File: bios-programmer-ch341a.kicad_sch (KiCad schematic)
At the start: 50 parts, among them J1 USB_B_Micro, J2 SPI Debug, J3 I²C Debug, J4 -Banana-, J5 +Banana+, J6 ZIF16, J7 Conn_02x05_Odd_Even, J8 Conn_02x05_Odd_Even, J9 SENSE, Q1 SSM3J328R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

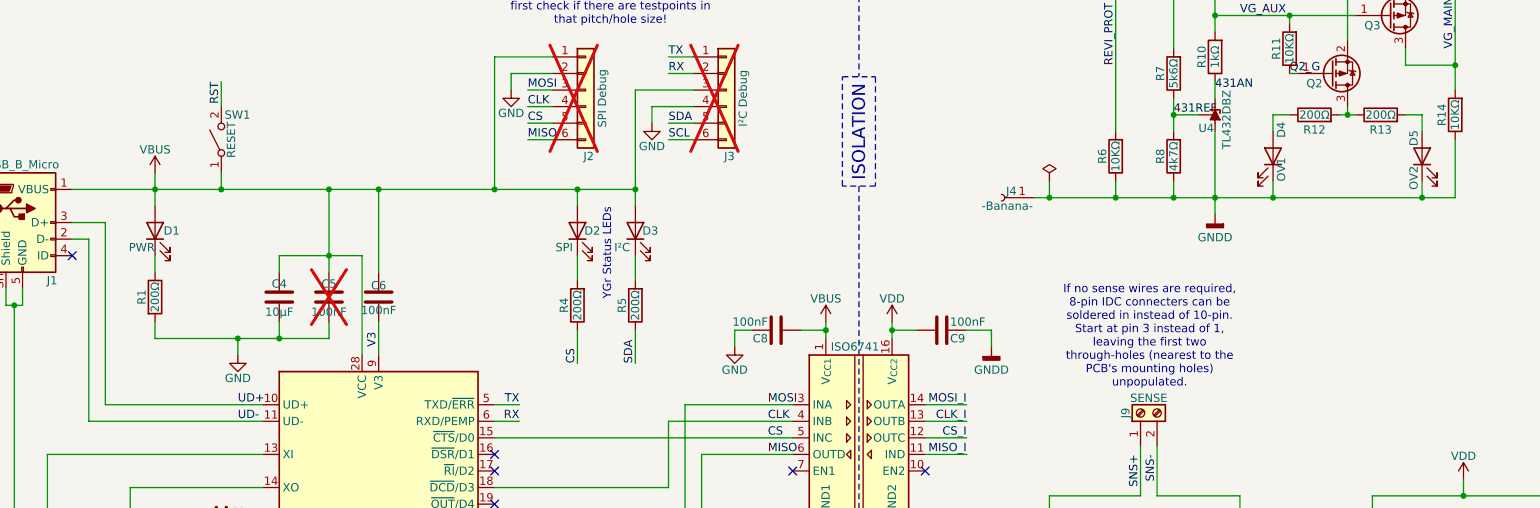
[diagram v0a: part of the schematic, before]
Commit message: PCB/SCH: separate field Label for PCB label & sort manufacturer/part #s
Using "Value" for the PCB label isn't terrible, but at the same time it's not
really "locked down" as a separate label. There's no reason Value can't be used
for something to indicate a certain message to the user in the schematics.
It's also not clear for anyone looking at the schematics that that specific
text is used on the PCB.

Splitting up removes any ambiguity.
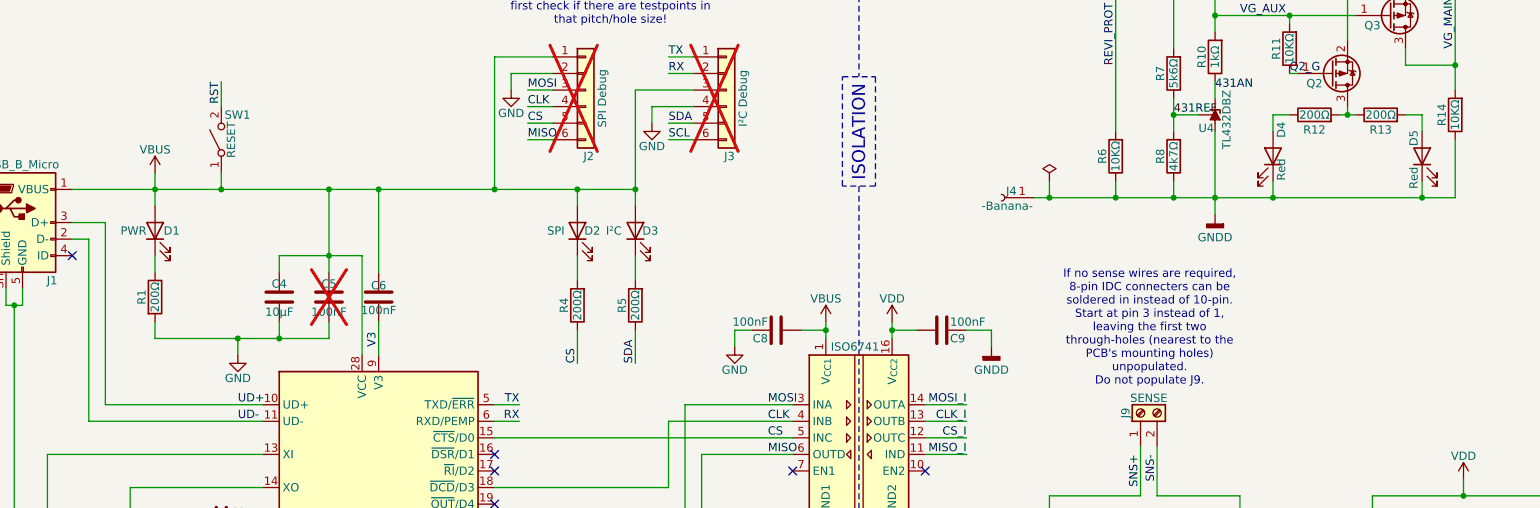
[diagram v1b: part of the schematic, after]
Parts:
- C1, C2: Manufacturer Kemet -> (none); Mfr (none) -> TODO calc; Part C0603C180F8HACAUTO -> TODO
- C3, C5, C6, C7, C8, C9: Mfr (none) -> Yageo; Part (none) -> CC0603KRX7R7BB104
- C4: Mfr (none) -> Taiyo Yuden; Part (none) -> JMK212B7106KG-T
- D1: value PWR -> TODO; Label (none) -> PWR
- D2: value SPI -> YellowGreen; Label (none) -> SPI; Mfr (none) -> Inolux; Part (none) -> HT-193UYG-5592
- D3: value I²C -> YellowGreen; Label (none) -> I²C; Mfr (none) -> Inolux; Part (none) -> HT-193UYG-5592
- D4: value OV1 -> Red
- D5: value OV2 -> Red
- J4: AltMfr1 (none) -> Schützinger; AltPart1 (none) -> 8094 TODO; Mfr (none) -> Cliff; Part (none) -> FCR7350B
- J5: AltMfr1 (none) -> Schützinger; AltPart1 (none) -> 8094 TODO; Mfr (none) -> Cliff; Part (none) -> FCR7350R
- J6: Mfr (none) -> M3
- R1, R12, R13, R4, R5: Mfr (none) -> Panasonic; Part (none) -> ERJ-3EKF2000V
- R11, R14, R6: Mfr (none) -> Yageo; Part (none) -> RC0603JR-0710KL
- SW1: value RESET -> SPST; Label (none) -> RESET
- U2: Part (none) -> ISO6741DWR
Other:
- note removed: "YGr Status LEDs"

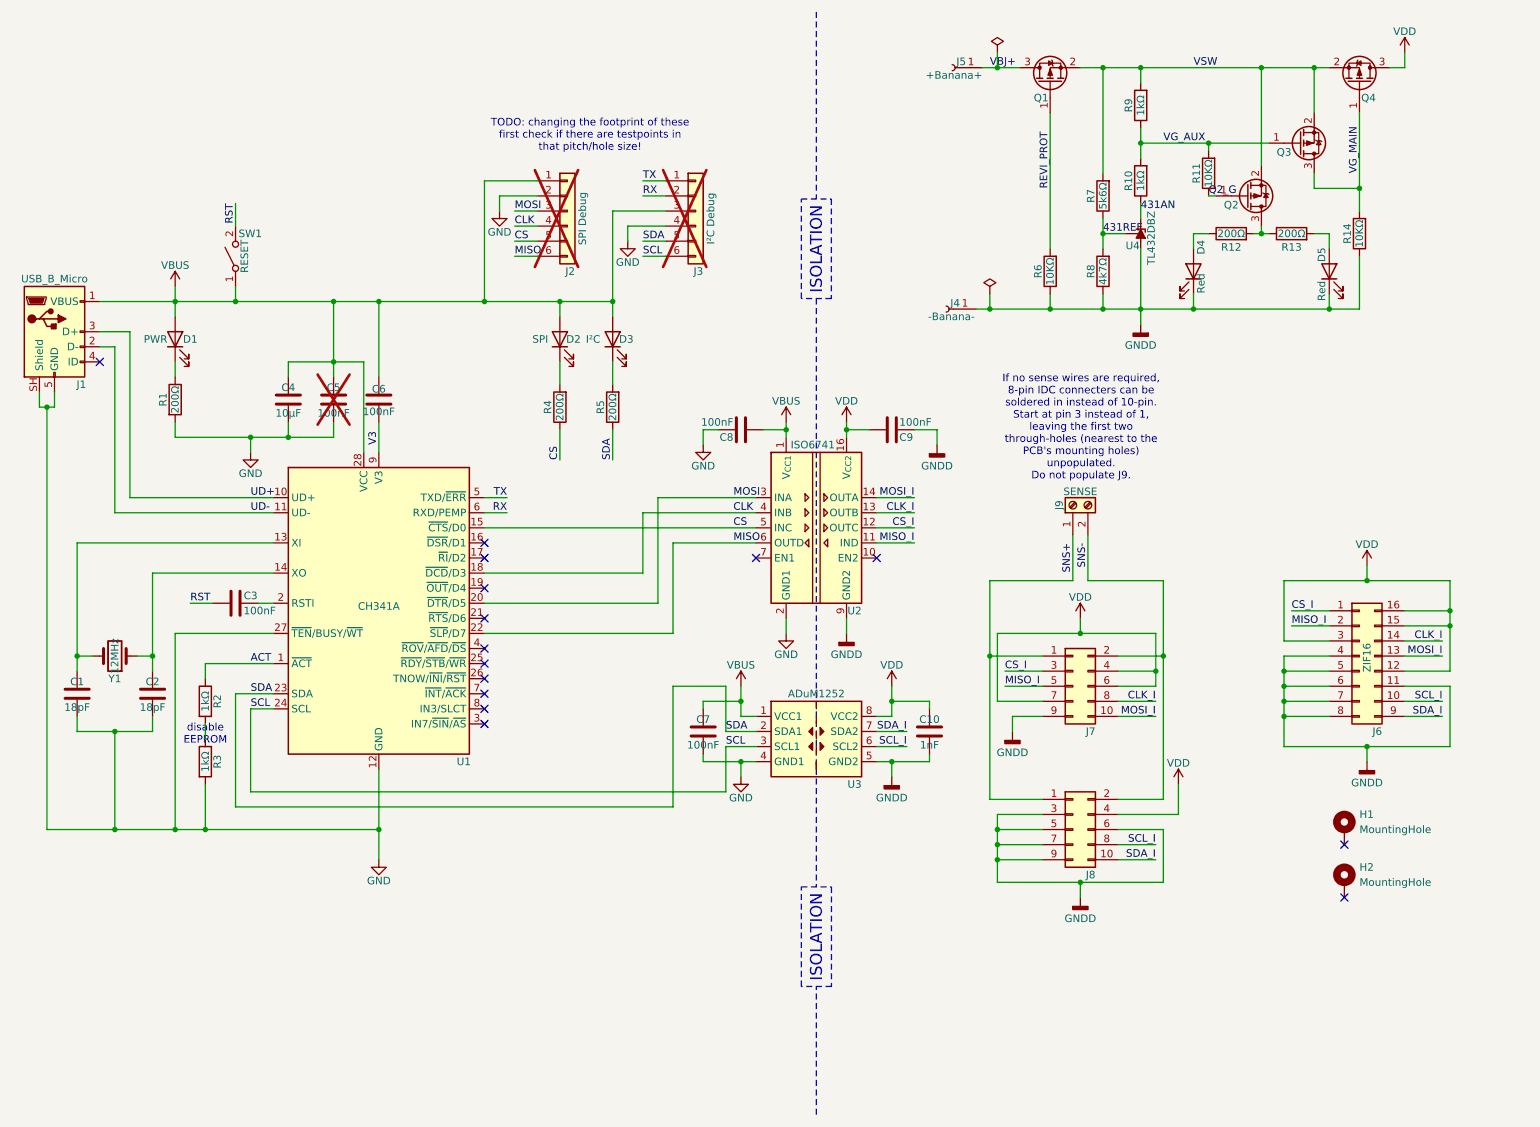
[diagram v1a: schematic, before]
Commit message: SCH: added some part numbers
Some part numbers have many possibilities, like 5% resistors. I assign these
simply based on what I have in stock, sometimes using a more expensive one that
uses up some of my (already very small) stock.
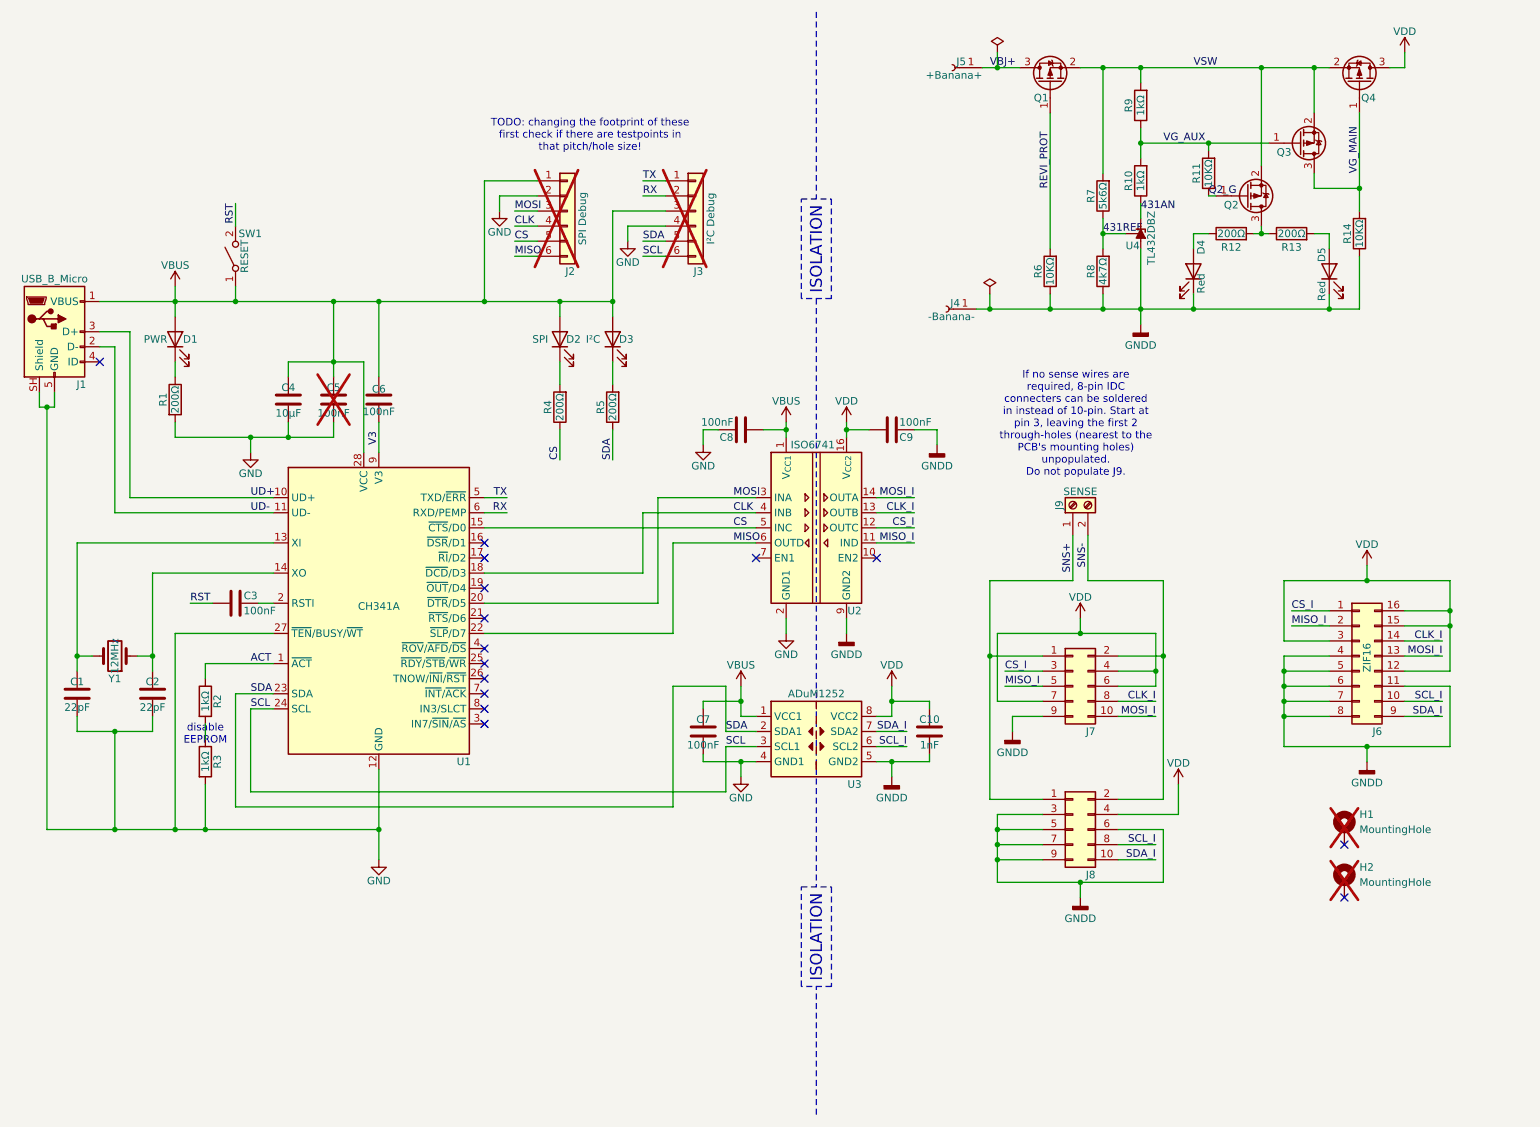
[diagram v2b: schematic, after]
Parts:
- C1, C2: value 18pF -> 22pF; AltMfr1 (none) -> Yageo; AltPart1 (none) -> CC0603GRNPO9BN220; Mfr TODO calc -> Kyocera / AVX; Part TODO -> 06035A270GAT2A
- C10: AltMfr1 (none) -> Samsung; AltPart1 (none) -> CL10B102KB8NNNC; Mfr (none) -> Murata; Part (none) -> GRM033R71H102KA12D
- D1: value TODO -> Blue; AltMfr1 (none) -> Lite-On Inc; AltPart1 (none) -> LTST-C170TBKT; Mfr (none) -> Inolux; Part (none) -> IN-S85AT5B
- D4, D5: AltMfr1 (none) -> Lite-On Inc; AltPart1 (none) -> LTST-C171KRKT; Mfr (none) -> Kingbright; Part (none) -> APT2012SURCK
- H1, H2: now not fitted
- J4: AltPart1 8094 TODO -> SWEB 8094 AU / RT
- J5: AltPart1 8094 TODO -> SWEB 8094 AU / SW
- J6: Part (none) -> 216-3340-00-0602J
- J7, J8: AltMfr1 (none) -> Wurth Elektronik; AltPart1 (none) -> 61201021721; Mfr (none) -> TE Connectivity; Part (none) -> 1761682-3
- R10, R2, R3, R9: Mfr (none) -> Royalohm; Part (none) -> CQ03WAJ0102T5E
- R7: Mfr (none) -> Susumu; Part (none) -> RG1608P-562-D-T5
- R8: Mfr (none) -> Susumu; Part (none) -> RR0816P-4641-D-65H
- SW1: Mfr (none) -> C&K; Part (none) -> PTS636SKG25SMTR LFS
- U3: Mfr (none) -> Analog Devices; Part (none) -> ADUM1252ASA+
- Y1: AltMfr1 (none) -> Abracon; AltPart1 (none) -> ABL-12.000MHZ-N2X-T; Mfr (none) -> Abracon; Part (none) -> ABL-12.000MHZ-B2

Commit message: PCB: updated sense wire connector models, added U3 (ADum) caps & more part#s
Previously I used a model which sort-of fit but already included in Kicad, now
I use an actual model of what I can expect it to look like.

The capacitors on the I2C isolator were in the datasheet, but it seems I forgot
to duplicate them. I had somehow put the 100nF & 1nF on a different side of the
isolation barrier. According to the datasheet I should have both on each side.

Also some beautification of tracks.
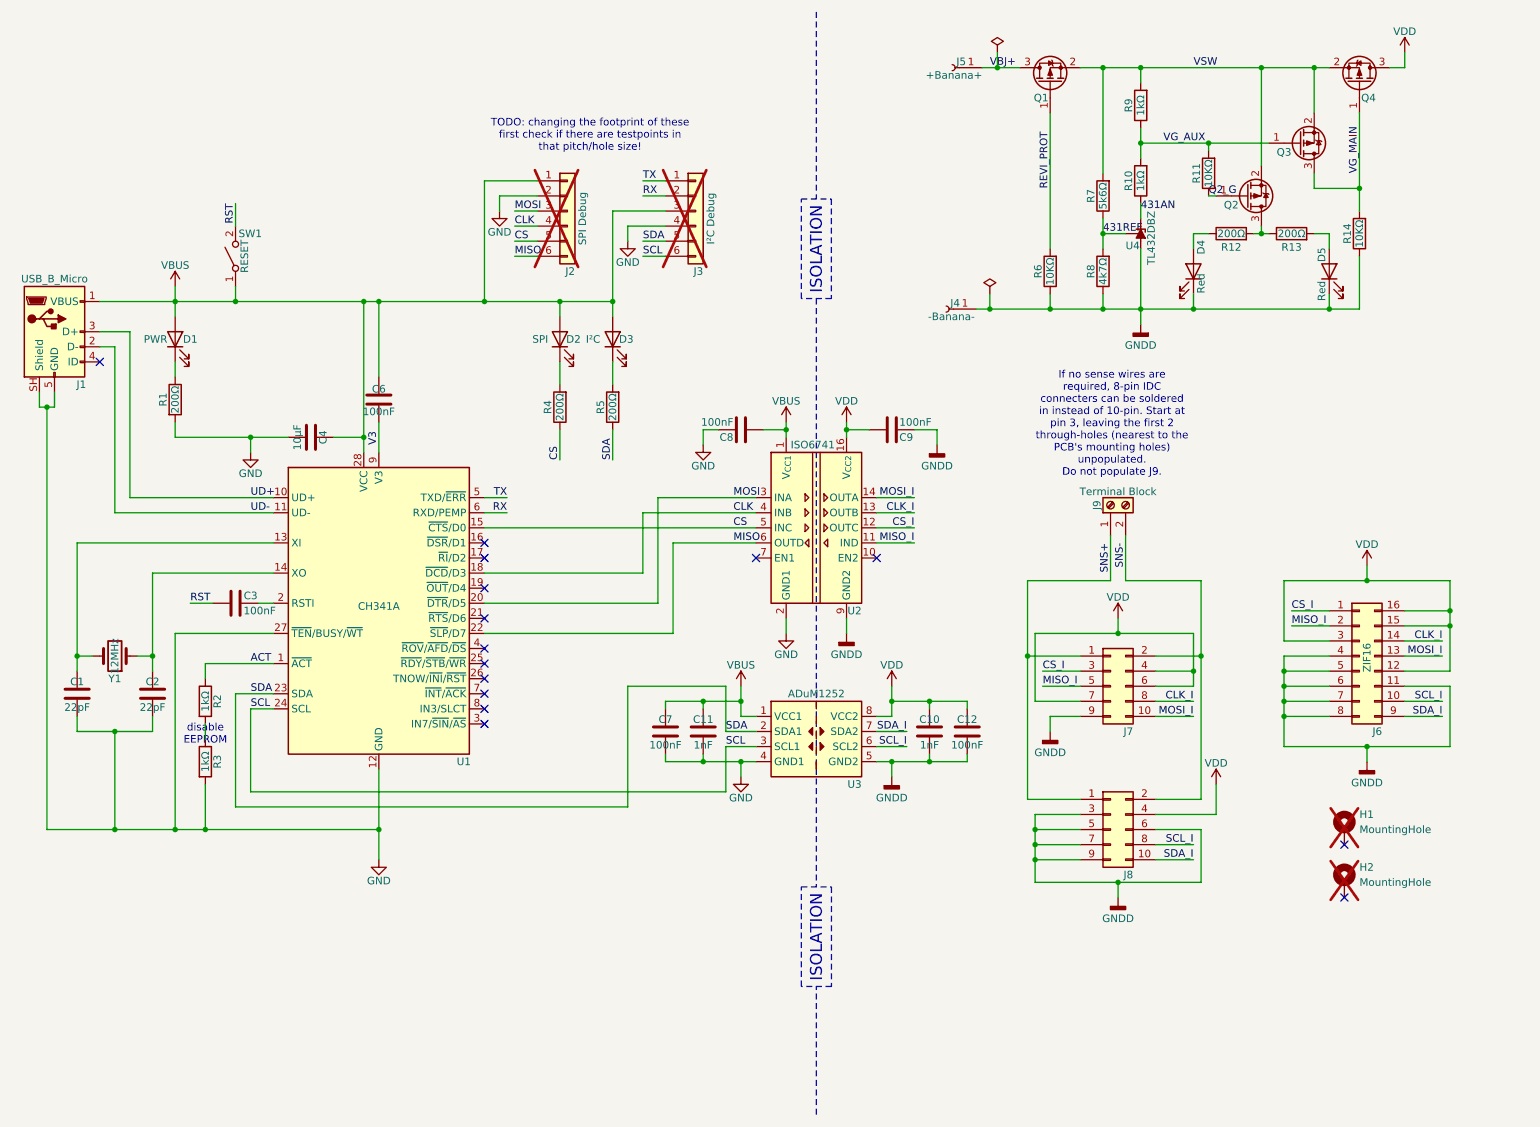
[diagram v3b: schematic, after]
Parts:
- removed C5: 100nF, Capacitor_SMD:C_0603_1608Metric_Pad1.08x0.95mm_HandSolder, symbol Device:C
- added C11: 1nF, Capacitor_SMD:C_0603_1608Metric_Pad1.08x0.95mm_HandSolder, symbol Device:C
- added C12: 100nF, Capacitor_SMD:C_0603_1608Metric_Pad1.08x0.95mm_HandSolder, symbol Device:C
- J4: AltPart1 SWEB 8094 AU / RT -> SWEB 8094 AU / SW
- J5: AltPart1 SWEB 8094 AU / SW -> SWEB 8094 AU / RT
- J7, J8: value Conn_02x05_Odd_Even -> IDC
- J9: value SENSE -> Terminal Block; AltMfr1 (none) -> Molex; AltPart1 (none) -> 39773-0002; Mfr (none) -> TE Connectivity; Part (none) -> 282834-2
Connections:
- net GND: now also C11.2
- net GNDD: now also C12.2
- net VBUS: now also C11.1
- net VDD: now also C12.1
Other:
- moved on the sheet: C4, C7, J7, J8, J9
